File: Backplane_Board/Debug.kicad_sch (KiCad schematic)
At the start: 4 parts, among them J44 Micro_SD_Card_Det2

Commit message: clean up
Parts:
- added TP1, TP2: TestPoint, TestPoint:TestPoint_Loop_D1.80mm_Drill1.0mm_Beaded, symbol Connector:TestPoint
- added TP3, TP4, TP6, TP7: TestPoint, TestPoint:TestPoint_Pad_2.5x2.5mm, symbol Connector:TestPoint
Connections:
- net +3.3V: now also TP7.1
- net I2C+: now also TP1.1
- net I2C-: now also TP2.1
- new net KillSW: TP6.1
- new net UART(RX): TP4.1
- new net UART(TX): TP3.1
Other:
- moved on the sheet: Brd1

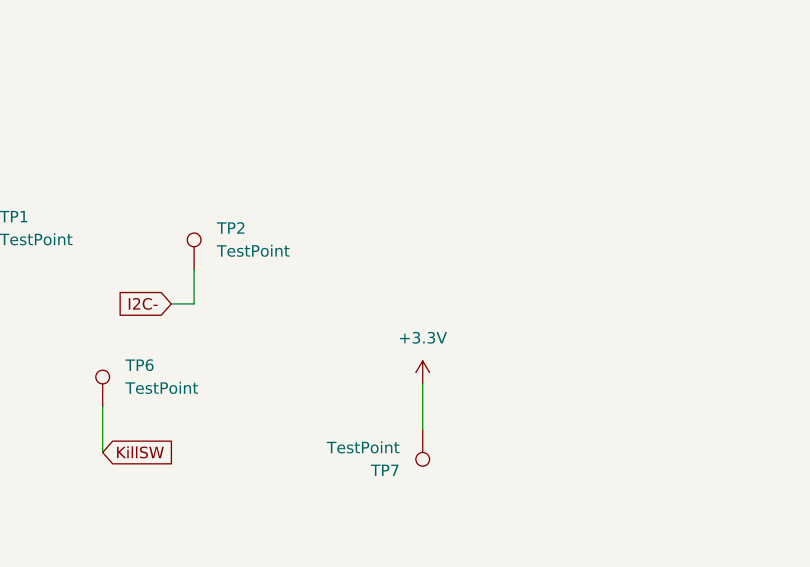
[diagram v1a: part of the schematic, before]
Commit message: add 3d modules and clean up footprints
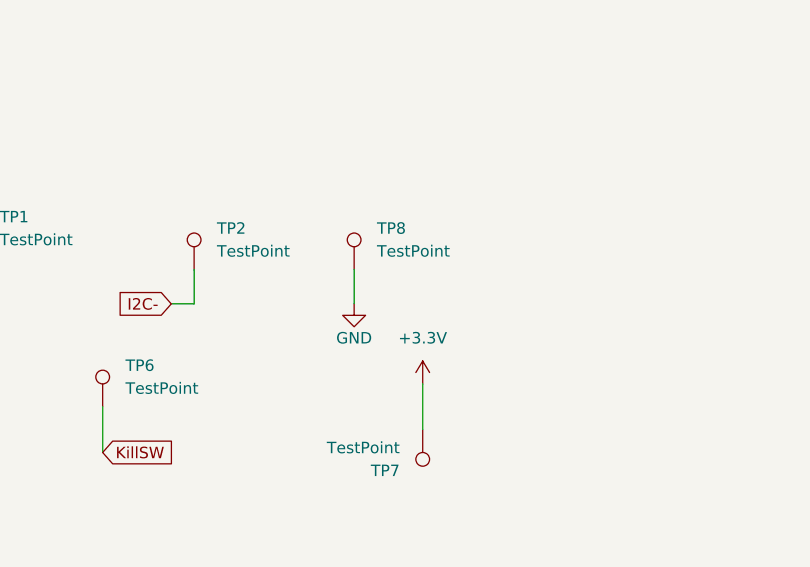
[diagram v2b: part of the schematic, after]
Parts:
- added TP8: TestPoint, TestPoint:TestPoint_Loop_D1.80mm_Drill1.0mm_Beaded, symbol Connector:TestPoint
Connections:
- net GND: now also TP8.1
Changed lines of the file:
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@@
+	(wire
+		(pts
+			(xy 96.52 133.35) (xy 96.52 137.16)
+		)
+		(stroke
+			(width 0)
+			(type default)
+		)
+	)
 	(wire
 		(pts
@@
 	)
 	(symbol
+		(lib_id "Connector:TestPoint")
+		(at 96.52 133.35 0)
+		(unit 1)
+		(exclude_from_sim no)
+		(in_bom yes)
+		(on_board yes)
+		(dnp no)
+		(fields_autoplaced yes)
+		(property "Reference" "TP8"
+			(at 99.06 128.7779 0)
+			(effects
+				(font
+					(size 1.27 1.27)
+				)
+				(justify left)
+			)
+		)
+		(property "Value" "TestPoint"
+			(at 99.06 131.3179 0)
+			(effects
+				(font
+					(size 1.27 1.27)
+				)
+				(justify left)
+			)
+		)
+		(property "Footprint" "TestPoint:TestPoint_Loop_D1.80mm_Drill1.0mm_Beaded"
+			(at 101.6 133.35 0)
+			(effects
+				(font
+					(size 1.27 1.27)
+				)
+				(hide yes)
+			)
+		)
+		(property "Datasheet" "~"
+			(at 101.6 133.35 0)
+			(effects
+				(font
+					(size 1.27 1.27)
+				)
+				(hide yes)
+			)
+		)
+		(property "Description" "test point"
+			(at 96.52 133.35 0)
+			(effects
+				(font
+					(size 1.27 1.27)
+				)
+				(hide yes)
+			)
+		)
+		(pin "1"
+		)
+		(instances
+			(project "Backplane_Board"
+				(path "/4484cfee-9e43-4cef-88b4-a8ca308542b4/5bff8e4d-59c9-4f86-b140-0d3398ae831d"
+					(reference "TP8")
+					(unit 1)
+				)
+			)
+		)
+	)
+	(symbol
 		(lib_id "Device:C")
 		(at 215.9 55.88 0)
@@
 					(unit 1)
 				)
+			)
+		)
+	)
+	(symbol
+		(lib_id "power:GND")
+		(at 96.52 137.16 0)
+		(unit 1)
+		(exclude_from_sim no)
+		(in_bom yes)
+		(on_board yes)
+		(dnp no)
+		(property "Reference" "#PWR0124"
+			(at 96.52 143.51 0)
+			(effects
+				(font
+					(size 1.27 1.27)
+				)
+				(hide yes)
+			)
+		)
+		(property "Value" "GND"
+			(at 96.52 140.97 0)
+			(effects
+				(font
+					(size 1.27 1.27)
+				)
+			)
+		)
+		(property "Footprint" ""
+			(at 96.52 137.16 0)
+			(effects
+				(font
+					(size 1.27 1.27)
+				)
+				(hide yes)
+			)
+		)
+		(property "Datasheet" ""
+			(at 96.52 137.16 0)
+			(effects
+				(font
+					(size 1.27 1.27)
+				)
+				(hide yes)
+			)
+		)
+		(property "Description" "Power symbol creates a global label with name \"GND\" , ground"
+			(at 96.52 137.16 0)
+			(effects
+				(font
+					(size 1.27 1.27)
+				)
+				(hide yes)
+			)
+		)
+		(pin "1"
+		)
+		(instances
+			(project ""
+				(path "/4484cfee-9e43-4cef-88b4-a8ca308542b4/5bff8e4d-59c9-4f86-b140-0d3398ae831d"
+					(reference "#PWR0124")
+					(unit 1)
+				)

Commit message: add anotations
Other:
- moved on the sheet: C27, J44, R51
